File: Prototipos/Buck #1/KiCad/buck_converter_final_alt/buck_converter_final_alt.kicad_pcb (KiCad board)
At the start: 2 copper layers, 50 x 100 mm, 52 parts, among them J2 Screw_Terminal_01x02, J3 Screw_Terminal_01x02, K1 SANYOU_SRD_Form_C, M5_BotL MountingHole_5.3mm_M5, M5_BotR MountingHole_5.3mm_M5, M5_TopL MountingHole_5.3mm_M5, M5_TopR MountingHole_5.3mm_M5, Q1 NPN, Q2 IRF9540NPBF, Q3 BC548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

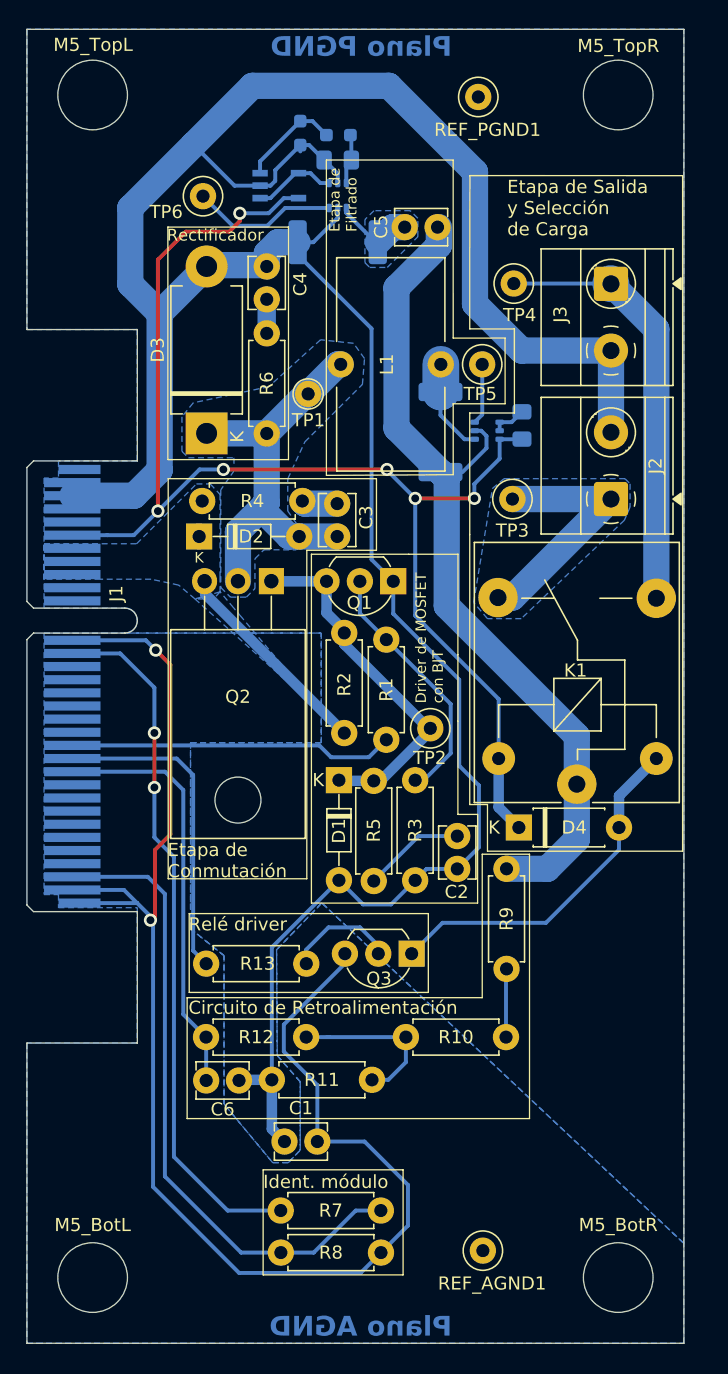
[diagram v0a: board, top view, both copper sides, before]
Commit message: Corregir relleno y traza 5V
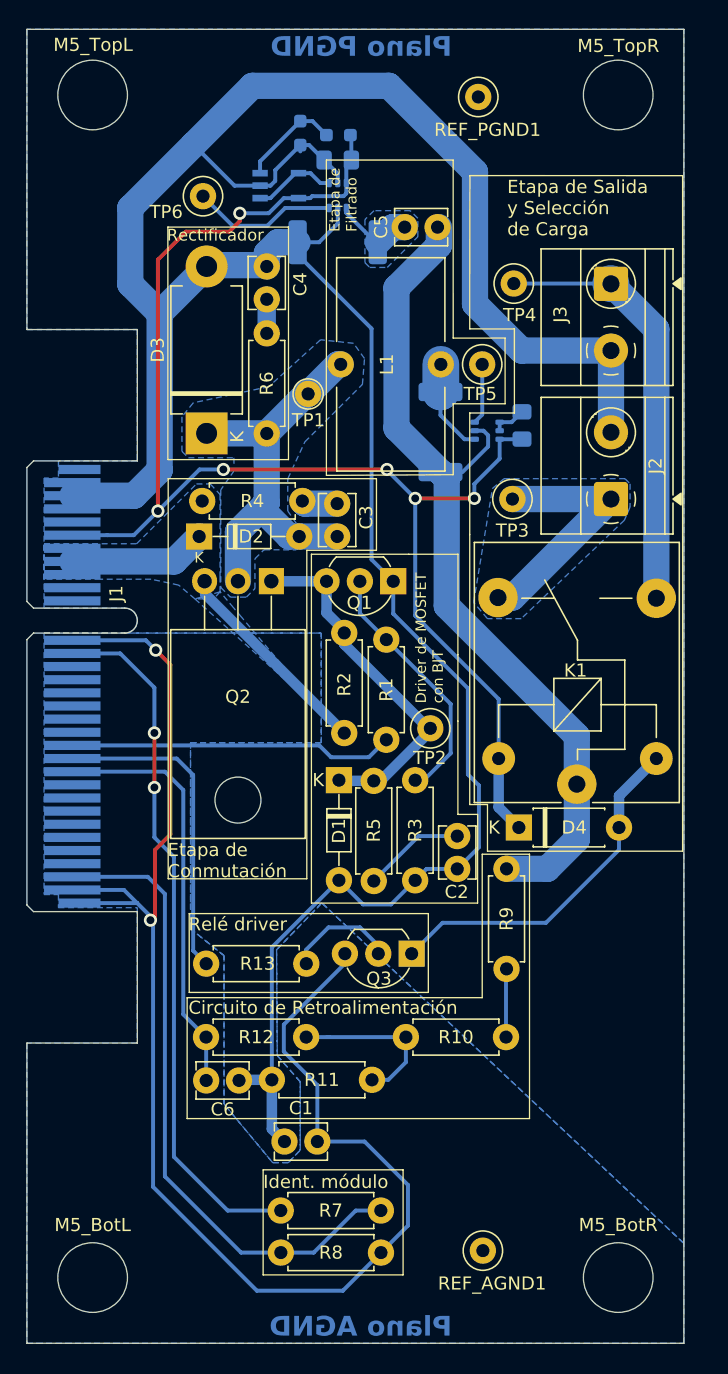
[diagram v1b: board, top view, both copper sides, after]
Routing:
- net 12V: track 16.0 -> 26.4 mm
- net 5Vdc: track 104.9 -> 109.5 mm
- net AGND: track 112.5 -> 113.6 mm
